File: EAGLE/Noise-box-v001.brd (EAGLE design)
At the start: 160 x 100 mm, 20 parts, among them J1 AVR_SPI_PROG_3X22X3_LOCK, J2 BATT, U1 ATMEGA328P_TQFP, U2 MIC5219 3.3V, U3 MCP73831

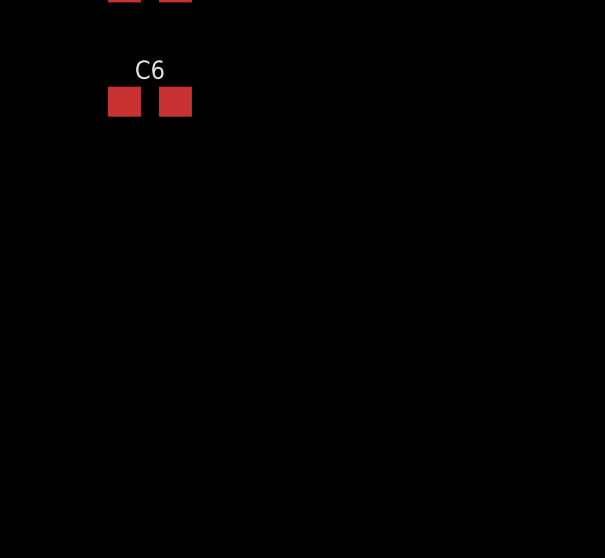
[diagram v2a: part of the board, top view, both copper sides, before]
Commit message: Low voltage rail
Added 1.8V rail to accomodate codec IC core
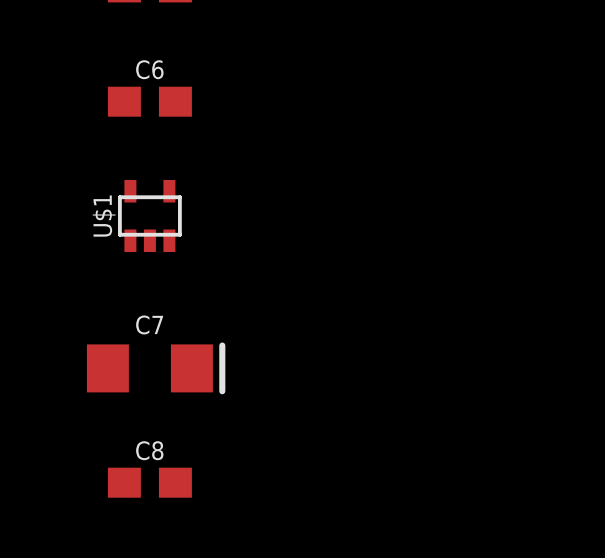
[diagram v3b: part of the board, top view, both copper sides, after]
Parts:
- added C7: 10uF, SparkFun-Capacitors:EIA3216
- added C8: 0.1uF, SparkFun-Capacitors:0603
- added U$1: 1.8V/100mA, SparkFun-IC-Power:SC70
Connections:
- new net VCC: C7.+, C8.1, U$1.5
- net +3V3: now also U$1.1, U$1.3
- net GND: now also C7.-, C8.2, U$1.2
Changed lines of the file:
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@@
 <attribute name="PROD_ID" value="CAP-08280" x="-33.02" y="-67.31" size="1.778" layer="27" display="off"/>
+</element>
+<element name="U$1" library="SparkFun-IC-Power" package="SC70" value="1.8V/100mA" x="-33.02" y="-71.12">
+<attribute name="PROD_ID" value="VREG-08428" x="-33.02" y="-71.12" size="1.778" layer="27" display="off"/>
+</element>
+<element name="C7" library="SparkFun-Capacitors" package="EIA3216" value="10uF" x="-33.02" y="-76.2">
+<attribute name="PROD_ID" value="CAP-00811" x="-33.02" y="-76.2" size="1.778" layer="27" display="off"/>
+</element>
+<element name="C8" library="SparkFun-Capacitors" package="0603" value="0.1uF" x="-33.02" y="-80.01">
+<attribute name="PROD_ID" value="CAP-08604" x="-33.02" y="-80.01" size="1.778" layer="27" display="off"/>
 </element>
 </elements>
@@
 <contactref element="C4" pad="1"/>
 <contactref element="D2" pad="A"/>
+<contactref element="U$1" pad="1"/>
+<contactref element="U$1" pad="3"/>
+<wire x1="-32.37" y1="-71.945" x2="-33.67" y2="-71.945" width="0" layer="19" extent="1-1"/>
+<wire x1="-22.29" y1="-40.64" x2="-32.37" y2="-71.945" width="0" layer="19" extent="1-1"/>
 <wire x1="-21.17" y1="-34.29" x2="-22.29" y2="-40.64" width="0" layer="19" extent="1-1"/>
 <wire x1="-21.17" y1="-30.48" x2="-21.17" y2="-34.29" width="0" layer="19" extent="1-1"/>
@@
 <contactref element="R4" pad="1"/>
 <contactref element="C6" pad="2"/>
+<contactref element="C7" pad="-"/>
+<contactref element="C8" pad="2"/>
+<contactref element="U$1" pad="2"/>
+<wire x1="-32.17" y1="-80.01" x2="-34.42" y2="-76.2" width="0" layer="19" extent="1-1"/>
+<wire x1="-33.02" y1="-71.945" x2="-34.42" y2="-76.2" width="0" layer="19" extent="1-1"/>
+<wire x1="-32.17" y1="-67.31" x2="-33.02" y2="-71.945" width="0" layer="19" extent="1-1"/>
+<wire x1="-33.87" y1="-63.5" x2="-32.17" y2="-67.31" width="0" layer="19" extent="1-1"/>
 <wire x1="-33.87" y1="-59.69" x2="-33.87" y2="-63.5" width="0" layer="19" extent="1-1"/>
-<wire x1="-32.17" y1="-67.31" x2="-33.87" y2="-63.5" width="0" layer="19" extent="1-1"/>
 <wire x1="-32.17" y1="-55.88" x2="-33.87" y2="-59.69" width="0" layer="19" extent="1-1"/>
 <wire x1="-34.29" y1="-40.6701" x2="-32.17" y2="-55.88" width="0" layer="19" extent="1-1"/>
@@
 <wire x1="-35.24" y1="-38.0699" x2="-32.17" y2="-59.69" width="0" layer="19" extent="1-1"/>
 </signal>
+<signal name="VCC">
+<contactref element="U$1" pad="5"/>
+<contactref element="C7" pad="+"/>
+<contactref element="C8" pad="1"/>
+<wire x1="-31.62" y1="-76.2" x2="-33.87" y2="-80.01" width="0" layer="19" extent="1-1"/>
+<wire x1="-33.67" y1="-70.295" x2="-31.62" y2="-76.2" width="0" layer="19" extent="1-1"/>
+</signal>
 </signals>

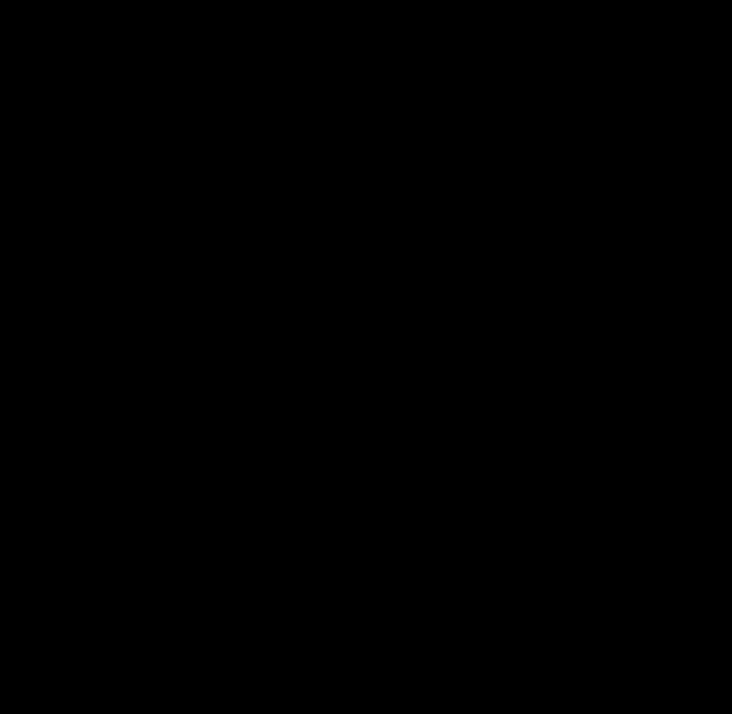
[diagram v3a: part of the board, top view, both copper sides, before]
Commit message: micro sd
Added micro sd socket, to hold music tracks
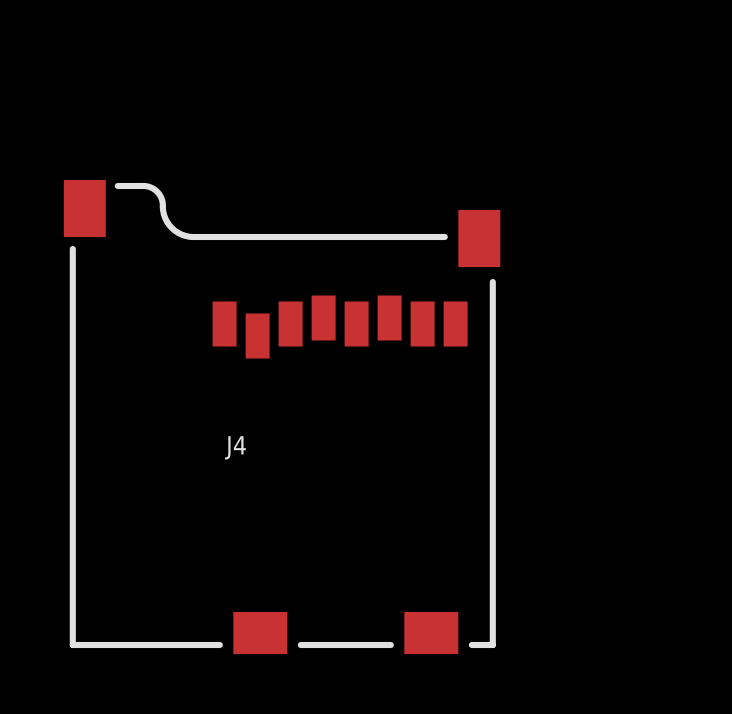
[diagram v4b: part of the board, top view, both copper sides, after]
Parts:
- added J4: MICRO-SD_CARD_SOCKET, SparkFun-Connectors:MICRO-SD-SOCKET
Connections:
- new net SD-CS: J4.CS
- net +3V3: now also J4.VCC
- net GND: now also J4.CD1, J4.CD2, J4.GND, J4.GND1, J4.GND3
- net MISO: now also J4.DO
- net MOSI: now also J4.DI
- net SCK: now also J4.SCLK
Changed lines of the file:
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@@
 <attribute name="PROD_ID" value="CAP-08604" x="-33.02" y="-80.01" size="1.778" layer="27" display="off"/>
+</element>
+<element name="J4" library="SparkFun-Connectors" package="MICRO-SD-SOCKET" value="MICRO-SD_CARD_SOCKET" x="-21.59" y="-104.14">
+<attribute name="SF_ID" value="PRT-00127" x="-21.59" y="-104.14" size="1.778" layer="27" display="off"/>
+<attribute name="PROD_ID" value="CONN-07820" x="-21.59" y="-104.14" size="1.778" layer="27" display="off"/>
 </element>
 </elements>
@@
 <contactref element="U$1" pad="1"/>
 <contactref element="U$1" pad="3"/>
-<wire x1="-32.37" y1="-71.945" x2="-33.67" y2="-71.945" width="0" layer="19" extent="1-1"/>
+<contactref element="J4" pad="VCC"/>
+<wire x1="-32.37" y1="-71.945" x2="-27.23" y2="-93.24" width="0" layer="19" extent="1-1"/>
+<wire x1="-33.67" y1="-71.945" x2="-32.37" y2="-71.945" width="0" layer="19" extent="1-1"/>
 <wire x1="-22.29" y1="-40.64" x2="-32.37" y2="-71.945" width="0" layer="19" extent="1-1"/>
 <wire x1="-21.17" y1="-34.29" x2="-22.29" y2="-40.64" width="0" layer="19" extent="1-1"/>
@@
 <contactref element="C8" pad="2"/>
 <contactref element="U$1" pad="2"/>
-<wire x1="-32.17" y1="-80.01" x2="-34.42" y2="-76.2" width="0" layer="19" extent="1-1"/>
+<contactref element="J4" pad="GND3"/>
+<contactref element="J4" pad="GND"/>
+<contactref element="J4" pad="GND1"/>
+<contactref element="J4" pad="CD1"/>
+<contactref element="J4" pad="CD2"/>
+<wire x1="-23.64" y1="-103.74" x2="-29.34" y2="-103.74" width="0" layer="19" extent="1-1"/>
+<wire x1="-25.03" y1="-93.24" x2="-23.64" y2="-103.74" width="0" layer="19" extent="1-1"/>
+<wire x1="-22.04" y1="-90.59" x2="-25.03" y2="-93.24" width="0" layer="19" extent="1-1"/>
+<wire x1="-35.19" y1="-89.59" x2="-25.03" y2="-93.24" width="0" layer="19" extent="1-1"/>
+<wire x1="-32.17" y1="-80.01" x2="-35.19" y2="-89.59" width="0" layer="19" extent="1-1"/>
+<wire x1="-34.42" y1="-76.2" x2="-32.17" y2="-80.01" width="0" layer="19" extent="1-1"/>
 <wire x1="-33.02" y1="-71.945" x2="-34.42" y2="-76.2" width="0" layer="19" extent="1-1"/>
 <wire x1="-32.17" y1="-67.31" x2="-33.02" y2="-71.945" width="0" layer="19" extent="1-1"/>
@@
 <signal name="MOSI">
 <contactref element="J1" pad="4"/>
+<contactref element="J4" pad="DI"/>
+<wire x1="-5.08" y1="-2.667" x2="-28.33" y2="-93.44" width="0" layer="19" extent="1-1"/>
 </signal>
 <signal name="RST">
@@
 <signal name="SCK">
 <contactref element="J1" pad="3"/>
+<contactref element="J4" pad="SCLK"/>
+<wire x1="-5.08" y1="-5.207" x2="-26.13" y2="-93.44" width="0" layer="19" extent="1-1"/>
 </signal>
 <signal name="MISO">
 <contactref element="J1" pad="1"/>
+<contactref element="J4" pad="DO"/>
+<wire x1="-7.62" y1="-4.953" x2="-23.93" y2="-93.44" width="0" layer="19" extent="1-1"/>
 </signal>
 <signal name="VBATT">
@@
 <wire x1="-33.67" y1="-70.295" x2="-31.62" y2="-76.2" width="0" layer="19" extent="1-1"/>
 </signal>
+<signal name="SD-CS">
+<contactref element="J4" pad="CS"/>
+</signal>
 </signals>

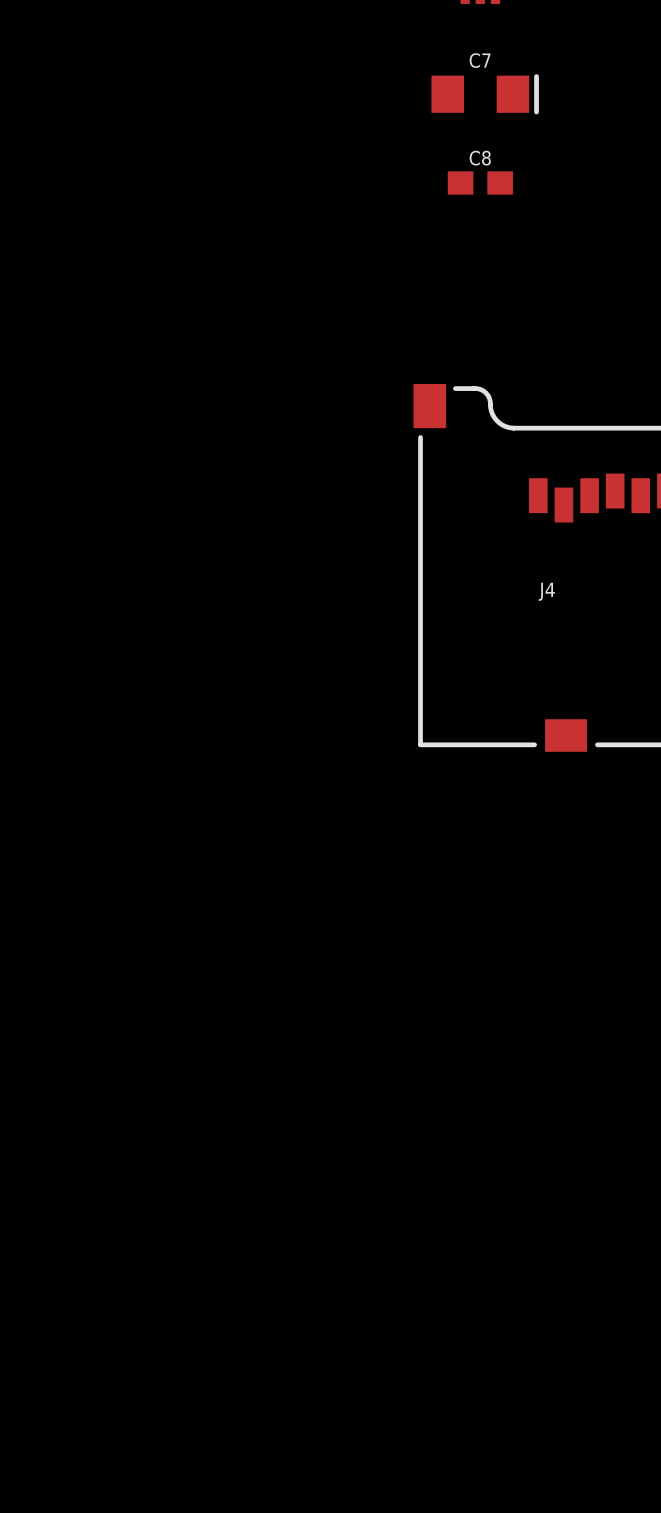
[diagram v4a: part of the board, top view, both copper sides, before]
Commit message: mp3 decoder
Added VL1063 codec, headphone jack
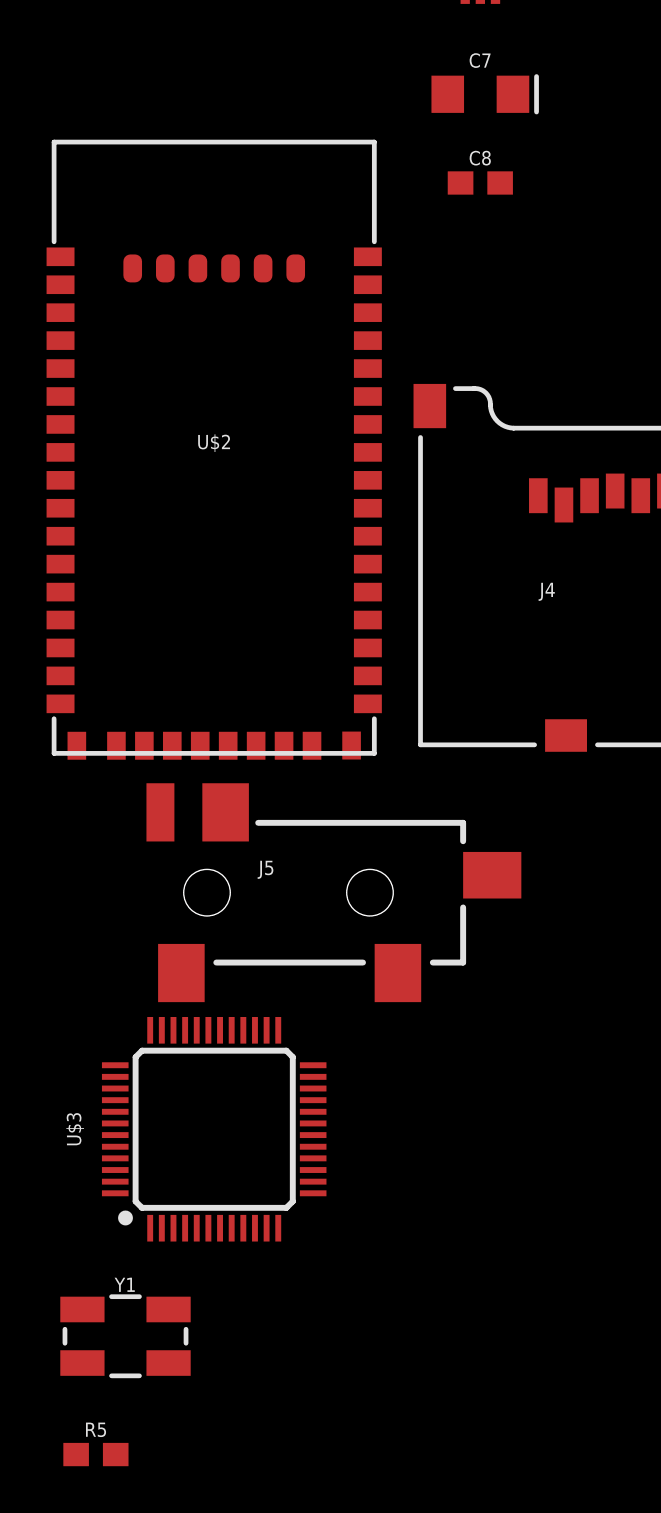
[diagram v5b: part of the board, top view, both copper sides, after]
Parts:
- added J5: AUDIO_JACK_3.5MM_SMD, SparkFun-Connectors:AUDIO-JACK-3.5MM-SMD
- added R5: 100k, SparkFun-Resistors:0603
- added U$2: BLUETOOTH-RN-52, SparkFun-RF:RN-52
- added U$3: VS1063SMD, SparkFun-IC-Conversion:LQFP-48
- added Y1: 12.288MHz, SparkFun-Clocks:CRYSTAL-SMD-5X3.2-4PAD
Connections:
- new net N$6: R5.2, U$3.10, U$3.11, U$3.12, U$3.9
- net GND: now also R5.1, U$3.16, U$3.20, U$3.21, U$3.22, U$3.35, U$3.37, U$3.4, U$3.40, U$3.41, U$3.47
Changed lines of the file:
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@@
 <attribute name="PROD_ID" value="CONN-07820" x="-21.59" y="-104.14" size="1.778" layer="27" display="off"/>
+</element>
+<element name="U$2" library="SparkFun-RF" package="RN-52" value="BLUETOOTH-RN-52" x="-44.45" y="-92.71">
+<attribute name="SF_ID" value="WRL-11678" x="-44.45" y="-92.71" size="1.778" layer="27" display="off"/>
+<attribute name="PROD_ID" value="IC-11569" x="-44.45" y="-92.71" size="1.778" layer="27" display="off"/>
+</element>
+<element name="J5" library="SparkFun-Connectors" package="AUDIO-JACK-3.5MM-SMD" value="AUDIO_JACK_3.5MM_SMD" x="-48.26" y="-110.49">
+<attribute name="PROD_ID" value="CONN-10353" x="-48.26" y="-110.49" size="1.778" layer="27" display="off"/>
+</element>
+<element name="U$3" library="SparkFun-IC-Conversion" package="LQFP-48" value="VS1063SMD" x="-44.45" y="-120.65">
+<attribute name="PROD_ID" value="IC-10870" x="-44.45" y="-120.65" size="1.778" layer="27" display="off"/>
+</element>
+<element name="Y1" library="SparkFun-Clocks" package="CRYSTAL-SMD-5X3.2-4PAD" value="12.288MHz" x="-48.26" y="-129.54">
+<attribute name="PROD_ID" value="XTAL-09653" x="-48.26" y="-129.54" size="1.778" layer="27" display="off"/>
+</element>
+<element name="R5" library="SparkFun-Resistors" package="0603" value="100k" x="-49.53" y="-134.62">
+<attribute name="PROD_ID" value="RES-07828" x="-49.53" y="-134.62" size="1.778" layer="27" display="off"/>
 </element>
 </elements>
@@
 <contactref element="J4" pad="CD1"/>
 <contactref element="J4" pad="CD2"/>
+<contactref element="U$3" pad="20"/>
+<contactref element="U$3" pad="4"/>
+<contactref element="U$3" pad="16"/>
+<contactref element="U$3" pad="21"/>
+<contactref element="U$3" pad="22"/>
+<contactref element="U$3" pad="35"/>
+<contactref element="U$3" pad="37"/>
+<contactref element="U$3" pad="40"/>
+<contactref element="U$3" pad="41"/>
+<contactref element="U$3" pad="47"/>
+<contactref element="R5" pad="1"/>
+<wire x1="-45.7" y1="-124.9" x2="-50.38" y2="-134.62" width="0" layer="19" extent="1-1"/>
+<wire x1="-48.7" y1="-122.9" x2="-45.7" y2="-124.9" width="0" layer="19" extent="1-1"/>
+<wire x1="-48.7" y1="-119.9" x2="-48.7" y2="-122.9" width="0" layer="19" extent="1-1"/>
+<wire x1="-48.7" y1="-119.4" x2="-48.7" y2="-119.9" width="0" layer="19" extent="1-1"/>
+<wire x1="-48.7" y1="-117.9" x2="-48.7" y2="-119.4" width="0" layer="19" extent="1-1"/>
+<wire x1="-46.7" y1="-116.4" x2="-48.7" y2="-117.9" width="0" layer="19" extent="1-1"/>
+<wire x1="-40.2" y1="-121.9" x2="-45.7" y2="-124.9" width="0" layer="19" extent="1-1"/>
+<wire x1="-40.2" y1="-119.9" x2="-40.2" y2="-121.9" width="0" layer="19" extent="1-1"/>
+<wire x1="-40.2" y1="-119.4" x2="-40.2" y2="-119.9" width="0" layer="19" extent="1-1"/>
+<wire x1="-40.2" y1="-118.9" x2="-40.2" y2="-119.4" width="0" layer="19" extent="1-1"/>
+<wire x1="-29.34" y1="-103.74" x2="-40.2" y2="-118.9" width="0" layer="19" extent="1-1"/>
 <wire x1="-23.64" y1="-103.74" x2="-29.34" y2="-103.74" width="0" layer="19" extent="1-1"/>
 <wire x1="-25.03" y1="-93.24" x2="-23.64" y2="-103.74" width="0" layer="19" extent="1-1"/>
@@
 <contactref element="J4" pad="CS"/>
 </signal>
+<signal name="N$6">
+<contactref element="U$3" pad="9"/>
+<contactref element="R5" pad="2"/>
+<contactref element="U$3" pad="10"/>
+<contactref element="U$3" pad="11"/>
+<contactref element="U$3" pad="12"/>
+<wire x1="-43.2" y1="-124.9" x2="-48.68" y2="-134.62" width="0" layer="19" extent="1-1"/>
+<wire x1="-42.7" y1="-124.9" x2="-43.2" y2="-124.9" width="0" layer="19" extent="1-1"/>
+<wire x1="-42.2" y1="-124.9" x2="-42.7" y2="-124.9" width="0" layer="19" extent="1-1"/>
+<wire x1="-41.7" y1="-124.9" x2="-42.2" y2="-124.9" width="0" layer="19" extent="1-1"/>
+</signal>
 </signals>
